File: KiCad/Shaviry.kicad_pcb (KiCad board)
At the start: 2 copper layers, 40.5 x 67.6 mm, 29 parts, among them J1 AMIGA_DB23_RGB_ENTRADA_HEMBRA, J2 VGA_SALIDA_HEMBRA, J3 VGA_ENTRADA_HEMBRA, J4 Conn_02x03_Top_Bottom, J5 Conn_01x03_Pin, U1 74HCT14, U3 THS7374, U5 PC817

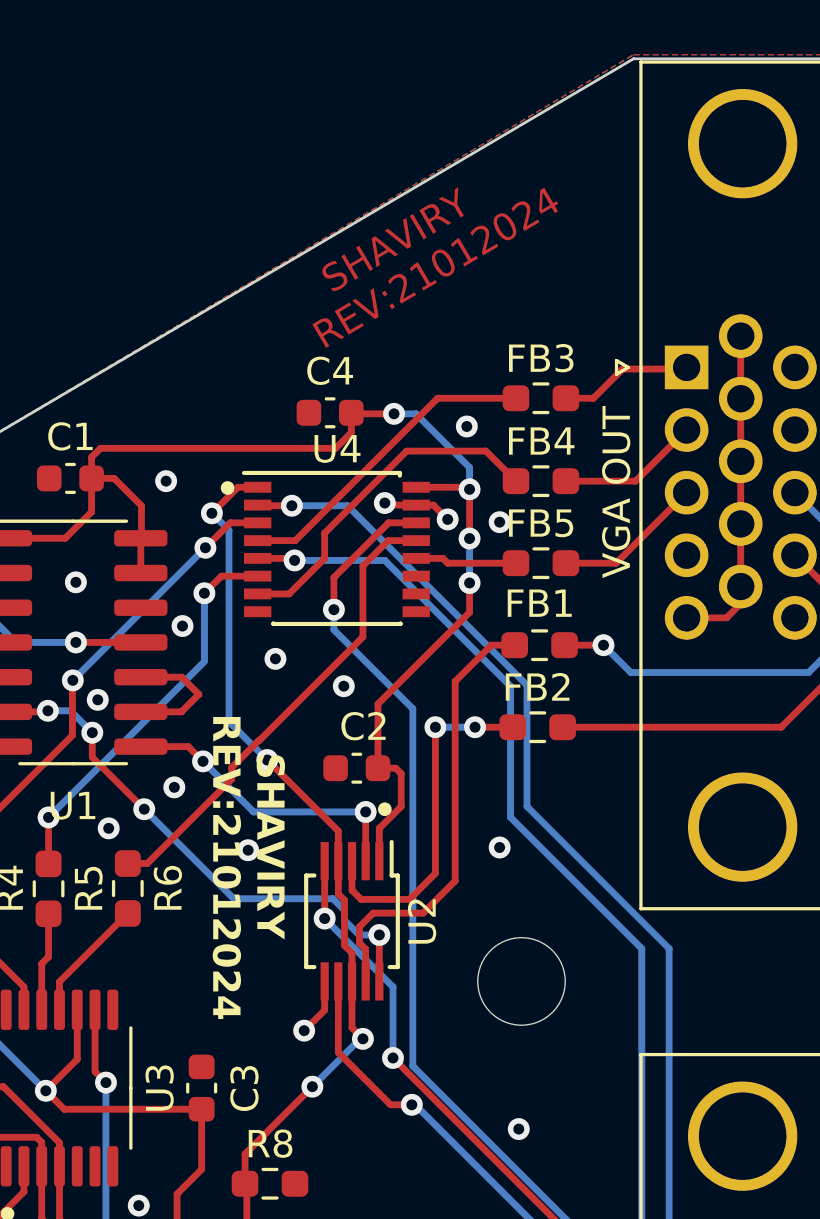
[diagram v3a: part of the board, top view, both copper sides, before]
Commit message: Add files via upload
Eliminadas todas las islas de masa sin conectar
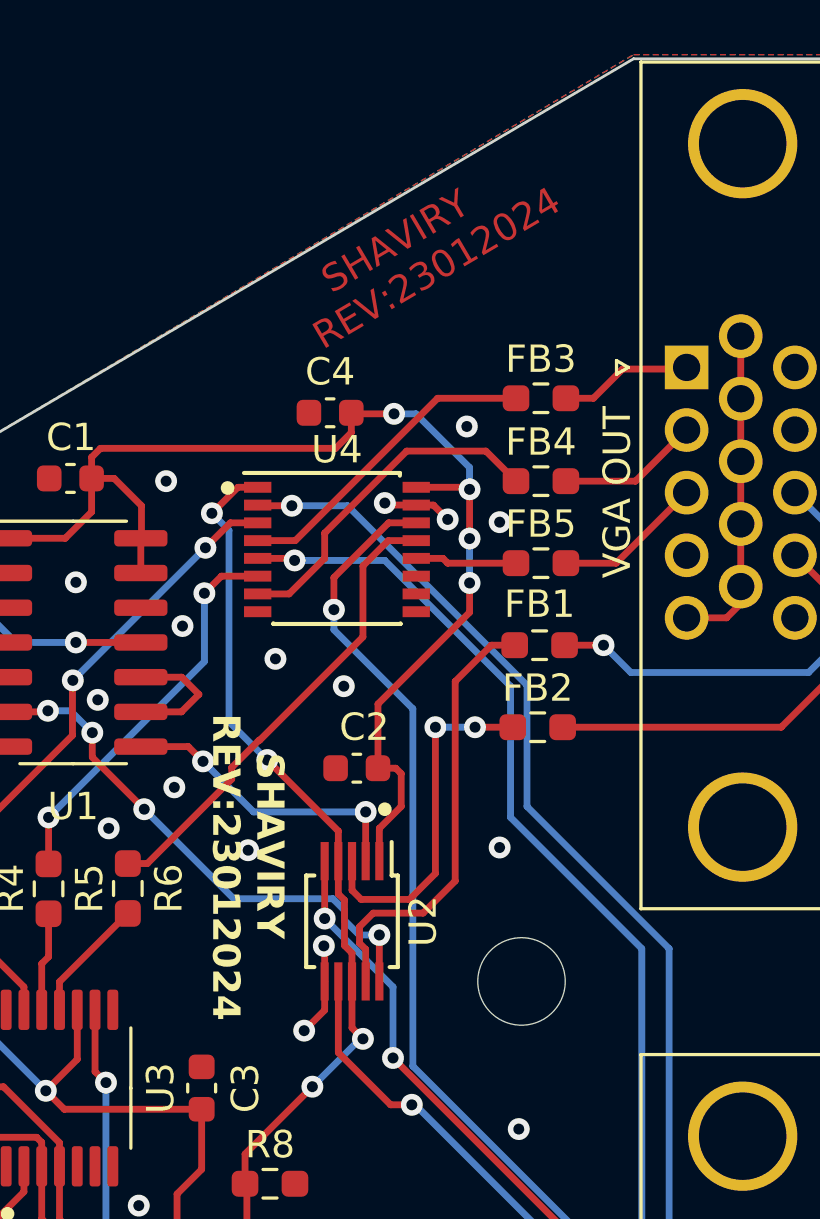
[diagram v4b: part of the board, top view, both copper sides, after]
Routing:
- net GND: track 28.5 -> 29.8 mm, vias 25 -> 26
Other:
- board text added: "SHAVIRY REV:23012024"
- board text removed: "SHAVIRY REV:21012024"
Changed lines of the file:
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@@
     )
     (stroke (width 0.1) (type solid)) (fill none) (layer "Edge.Cuts"))
-  (gr_text "   SHAVIRY\nREV:21012024" (at 146.7 64.945 30.5) (layer "F.Cu" knockout)
+  (gr_text "   SHAVIRY\nREV:23012024" (at 146.7 64.945 30.5) (layer "F.Cu" knockout)
     (effects (font (size 1 1) (thickness 0.15)) (justify left bottom))
   )
@@
     (effects (font (size 1 1) (thickness 0.15)) (justify left bottom))
   )
-  (gr_text "   SHAVIRY\nREV:21012024" (at 142.5 78.145 270) (layer "F.SilkS")
+  (gr_text "   SHAVIRY\nREV:23012024" (at 142.5 78.145 270) (layer "F.SilkS")
     (effects (font (size 1 1) (thickness 0.25) bold) (justify left bottom))
   )
@@
   (segment (start 145.95 89.745) (end 146.7 88.995) (width 0.25) (layer "F.Cu") (net 5))
   (segment (start 159.94 74.645) (end 161.4 74.645) (width 0.25) (layer "F.Cu") (net 5))
+  (segment (start 146.7 86.675) (end 146.67 86.645) (width 0.25) (layer "F.Cu") (net 5))
   (segment (start 161.185 110.95) (end 161.92 110.215) (width 0.25) (layer "F.Cu") (net 5))
+  (segment (start 146.7 87.945) (end 146.7 86.675) (width 0.25) (layer "F.Cu") (net 5))
   (segment (start 148.975 70.52) (end 148.9 70.445) (width 0.25) (layer "F.Cu") (net 5))
   (segment (start 159.94 110.95) (end 161.185 110.95) (width 0.25) (layer "F.Cu") (net 5))
@@
   (via (at 148.9 70.445) (size 0.8) (drill 0.4) (layers "F.Cu" "B.Cu") (free) (net 5))
   (via (at 138.8 82.345) (size 0.8) (drill 0.4) (layers "F.Cu" "B.Cu") (free) (net 5))
+  (via (at 146.67 86.645) (size 0.8) (drill 0.4) (layers "F.Cu" "B.Cu") (free) (net 5))
   (via (at 157.8 103.045) (size 0.8) (drill 0.4) (layers "F.Cu" "B.Cu") (free) (net 5))
   (via (at 139.9 96.145) (size 0.8) (drill 0.4) (layers "F.Cu" "B.Cu") (free) (net 5))
@@
   (segment (start 138.3 102.145) (end 138.7 101.745) (width 0.25) (layer "B.Cu") (net 67))
   (segment (start 138.7 101.745) (end 138.7 91.645) (width 0.25) (layer "B.Cu") (net 67))
+  (zone (net 0) (net_name "") (layer "F.Cu") (hatch edge 0.5)
+    (connect_pads (clearance 0))
+    (min_thickness 0.25) (filled_areas_thickness no)
+    (keepout (tracks allowed) (vias allowed) (pads allowed) (copperpour not_allowed) (footprints allowed))
+    (fill (thermal_gap 0.5) (thermal_bridge_width 0.5))
+    (polygon
+      (pts
+        (xy 143.43 71.825)
+        (xy 142.98 71.825)
+        (xy 142.98 72.735)
+        (xy 143.42 72.735)
+      )
+    )
+  )
+  (zone (net 0) (net_name "") (layer "F.Cu") (hatch edge 0.5)
+    (connect_pads (clearance 0))
+    (min_thickness 0.25) (filled_areas_thickness no)
+    (keepout (tracks allowed) (vias allowed) (pads allowed) (copperpour not_allowed) (footprints allowed))
+    (fill (thermal_gap 0.5) (thermal_bridge_width 0.5))
+    (polygon
+      (pts
+        (xy 151.8 68.935)
+        (xy 149.74 68.935)
+        (xy 149.74 69.415)
+        (xy 151.8 69.415)
+      )
+    )
+  )
+  (zone (net 0) (net_name "") (layer "F.Cu") (hatch edge 0.5)
+    (connect_pads (clearance 0))
+    (min_thickness 0.25) (filled_areas_thickness no)
+    (keepout (tracks allowed) (vias allowed) (pads allowed) (copperpour not_allowed) (footprints allowed))
+    (fill (thermal_gap 0.5) (thermal_bridge_width 0.5))
+    (polygon
+      (pts
+        (xy 133.71 72.785)
+        (xy 132.67 73.725)
+        (xy 134.03 73.715)
+      )
+    )
+  )
+  (zone (net 0) (net_name "") (layer "F.Cu") (hatch edge 0.5)
+    (connect_pads (clearance 0))
+    (min_thickness 0.25) (filled_areas_thickness no)
+    (keepout (tracks allowed) (vias allowed) (pads allowed) (copperpour not_allowed) (footprints allowed))
+    (fill (thermal_gap 0.5) (thermal_bridge_width 0.5))
+    (polygon
+      (pts
+        (xy 150.87 73.075)
+        (xy 150.87 74.725)
+        (xy 151.47 74.725)
+        (xy 151.47 73.075)
+      )
+    )
+  )
+  (zone (net 0) (net_name "") (layer "F.Cu") (hatch edge 0.5)
+    (connect_pads (clearance 0))
+    (min_thickness 0.25) (filled_areas_thickness no)
+    (keepout (tracks allowed) (vias allowed) (pads allowed) (copperpour not_allowed) (footprints allowed))
+    (fill (thermal_gap 0.5) (thermal_bridge_width 0.5))
+    (polygon
+      (pts
+        (xy 130.75 72.855)
+        (xy 130.75 74.755)
+        (xy 131.74 74.755)
+        (xy 131.26 73.805)
+        (xy 131.85 72.865)
+      )
+    )
+  )
+  (zone (net 0) (net_name "") (layer "F.Cu") (hatch edge 0.5)
+    (connect_pads (clearance 0))
+    (min_thickness 0.25) (filled_areas_thickness no)
+    (keepout (tracks allowed) (vias allowed) (pads allowed) (copperpour not_allowed) (footprints allowed))
+    (fill (thermal_gap 0.5) (thermal_bridge_width 0.5))
+    (polygon
+      (pts
+        (xy 137.81 91.195)
+        (xy 137.05 91.995)
+        (xy 138.26 92.245)
+      )
+    )
+  )
+  (zone (net 0) (net_name "") (layer "F.Cu") (hatch edge 0.5)
+    (connect_pads (clearance 0))
+    (min_thickness 0.25) (filled_areas_thickness no)
+    (keepout (tracks allowed) (vias allowed) (pads allowed) (copperpour not_allowed) (footprints allowed))
+    (fill (thermal_gap 0.5) (thermal_bridge_width 0.5))
+    (polygon
+      (pts
+        (xy 141.76 99.305)
+        (xy 142.47 99.745)
+        (xy 141.76 100.225)
+      )
+    )
+  )
+  (zone (net 0) (net_name "") (layer "F.Cu") (hatch edge 0.5)
+    (connect_pads (clearance 0))
+    (min_thickness 0.25) (filled_areas_thickness no)
+    (keepout (tracks allowed) (vias allowed) (pads allowed) (copperpour not_allowed) (footprints allowed))
+    (fill (thermal_gap 0.5) (thermal_bridge_width 0.5))
+    (polygon
+      (pts
+        (xy 149.02 91.425)
+        (xy 149.02 91.895)
+        (xy 149.47 91.895)
+        (xy 149.47 91.425)
+      )
+    )
+  )
   (zone (net 5) (net_name "GND") (layers "F&B.Cu") (hatch edge 0.5)
     (connect_pads (clearance 0.35))
@@
       )
     )
+  )
+  (zone (net 0) (net_name "") (layers "F&B.Cu") (hatch edge 0.5)
+    (connect_pads (clearance 0))
+    (min_thickness 0.25) (filled_areas_thickness no)
+    (keepout (tracks allowed) (vias allowed) (pads allowed) (copperpour not_allowed) (footprints allowed))
+    (fill (thermal_gap 0.5) (thermal_bridge_width 0.5))
+    (polygon
+      (pts
+        (xy 153.06 107.915)
+        (xy 153.34 107.925)
+        (xy 153.61 108.385)
+        (xy 154.01 108.675)
+        (xy 154.01 108.885)
+        (xy 153.44 109.205)
+        (xy 153.16 109.685)
+        (xy 153.16 110.485)
+        (xy 153.46 110.975)
+        (xy 154.02 111.345)
+        (xy 154.02 111.595)
+        (xy 153.67 111.765)
+        (xy 153.16 112.535)
+        (xy 153 112.535)
+        (xy 152.65 111.775)
+        (xy 152.07 111.475)
+        (xy 152.07 111.225)
+        (xy 152.57 110.985)
+        (xy 152.93 110.485)
+        (xy 152.93 109.635)
+        (xy 152.44 109.115)
+        (xy 152.17 108.995)
+        (xy 152.17 108.705)
+        (xy 152.8 108.705)
+        (xy 152.99 108.505)
+        (xy 153.01 107.915)
+      )
+    )
+  )
+  (zone (net 0) (net_name "") (layer "B.Cu") (hatch edge 0.5)
+    (connect_pads (clearance 0))
+    (min_thickness 0.25) (filled_areas_thickness no)
+    (keepout (tracks allowed) (vias allowed) (pads allowed) (copperpour not_allowed) (footprints allowed))
+    (fill (thermal_gap 0.5) (thermal_bridge_width 0.5))
+    (polygon
+      (pts
+        (xy 165.03 72.835)
+        (xy 164.2 73.535)
+        (xy 165.04 74.125)
+      )
+    )
+  )
+  (zone (net 0) (net_name "") (layer "B.Cu") (hatch edge 0.5)
+    (connect_pads (clearance 0))
+    (min_thickness 0.25) (filled_areas_thickness no)
+    (keepout (tracks allowed) (vias allowed) (pads allowed) (copperpour not_allowed) (footprints allowed))
+    (fill (thermal_gap 0.5) (thermal_bridge_width 0.5))
+    (polygon
+      (pts
+        (xy 149.48 86.605)
+        (xy 148.85 87.085)
+        (xy 149.47 87.655)
+      )
+    )
